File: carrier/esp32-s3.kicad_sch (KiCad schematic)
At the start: 16 parts, among them J1 USB_C_Receptacle_USB2.0, J5 ESP GPIO 1, J6 ESP GPIO 2, SW1 ESP RST, U2 ESP32-S3-MINI-1-N8, U5 TPD4EUSB30

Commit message: Feat[carrier]: v3 schematic draft complete
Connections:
- net USB2_N is gone; now on net USB_P: U5.4 (D2+), U5.7
- net USB2_P is gone; now on net USB_N: U5.5 (D2-), U5.6
- net ADC2_CH4: now reaches U2.19 (IO15)
- net ADC1_CH4: now reaches U2.9 (IO5)
- no-connect marks 28 -> 26
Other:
- moved on the sheet: C5, C6, C7, C8, C9, J1, J5, J6, R2, R3, R5, R8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

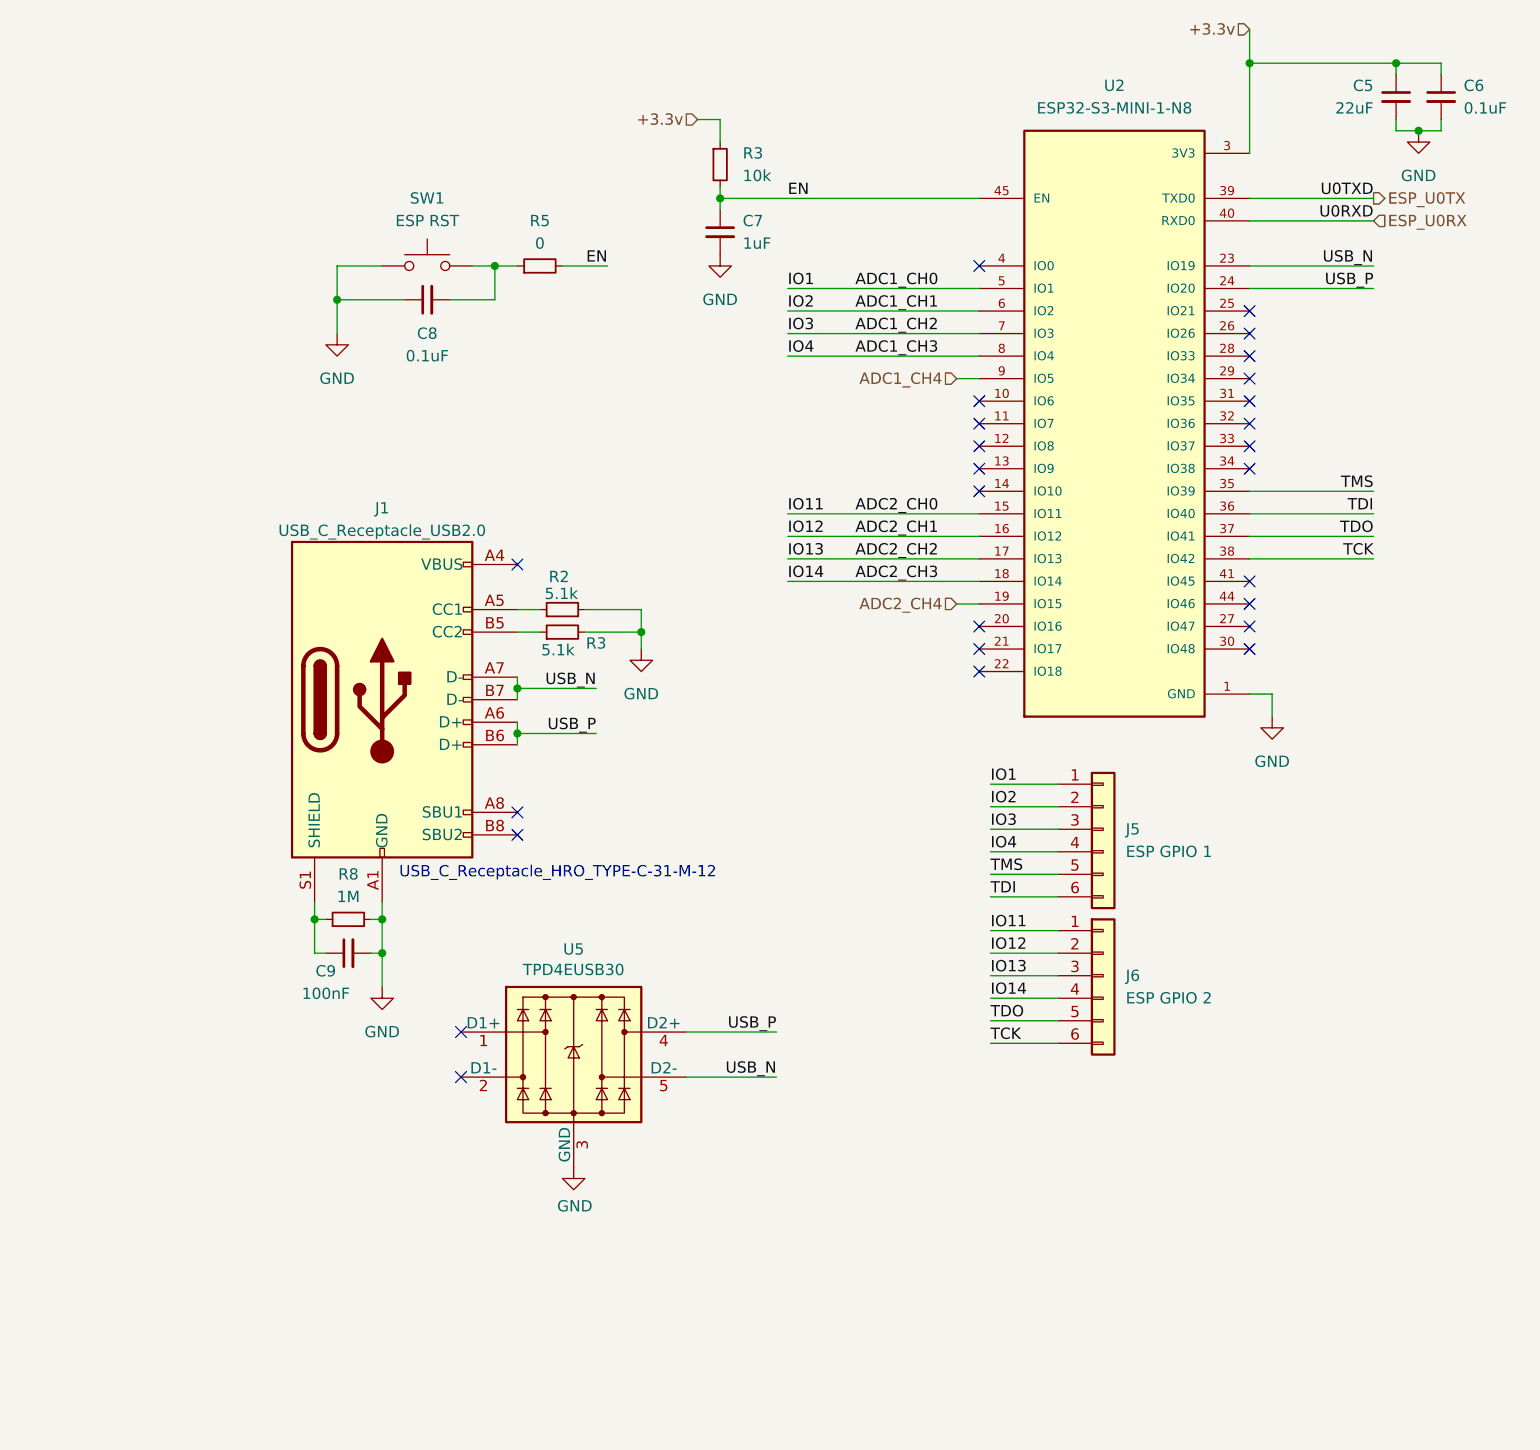
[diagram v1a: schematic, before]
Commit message: Feat[carrier]: implemented external magnetics, footprints linked
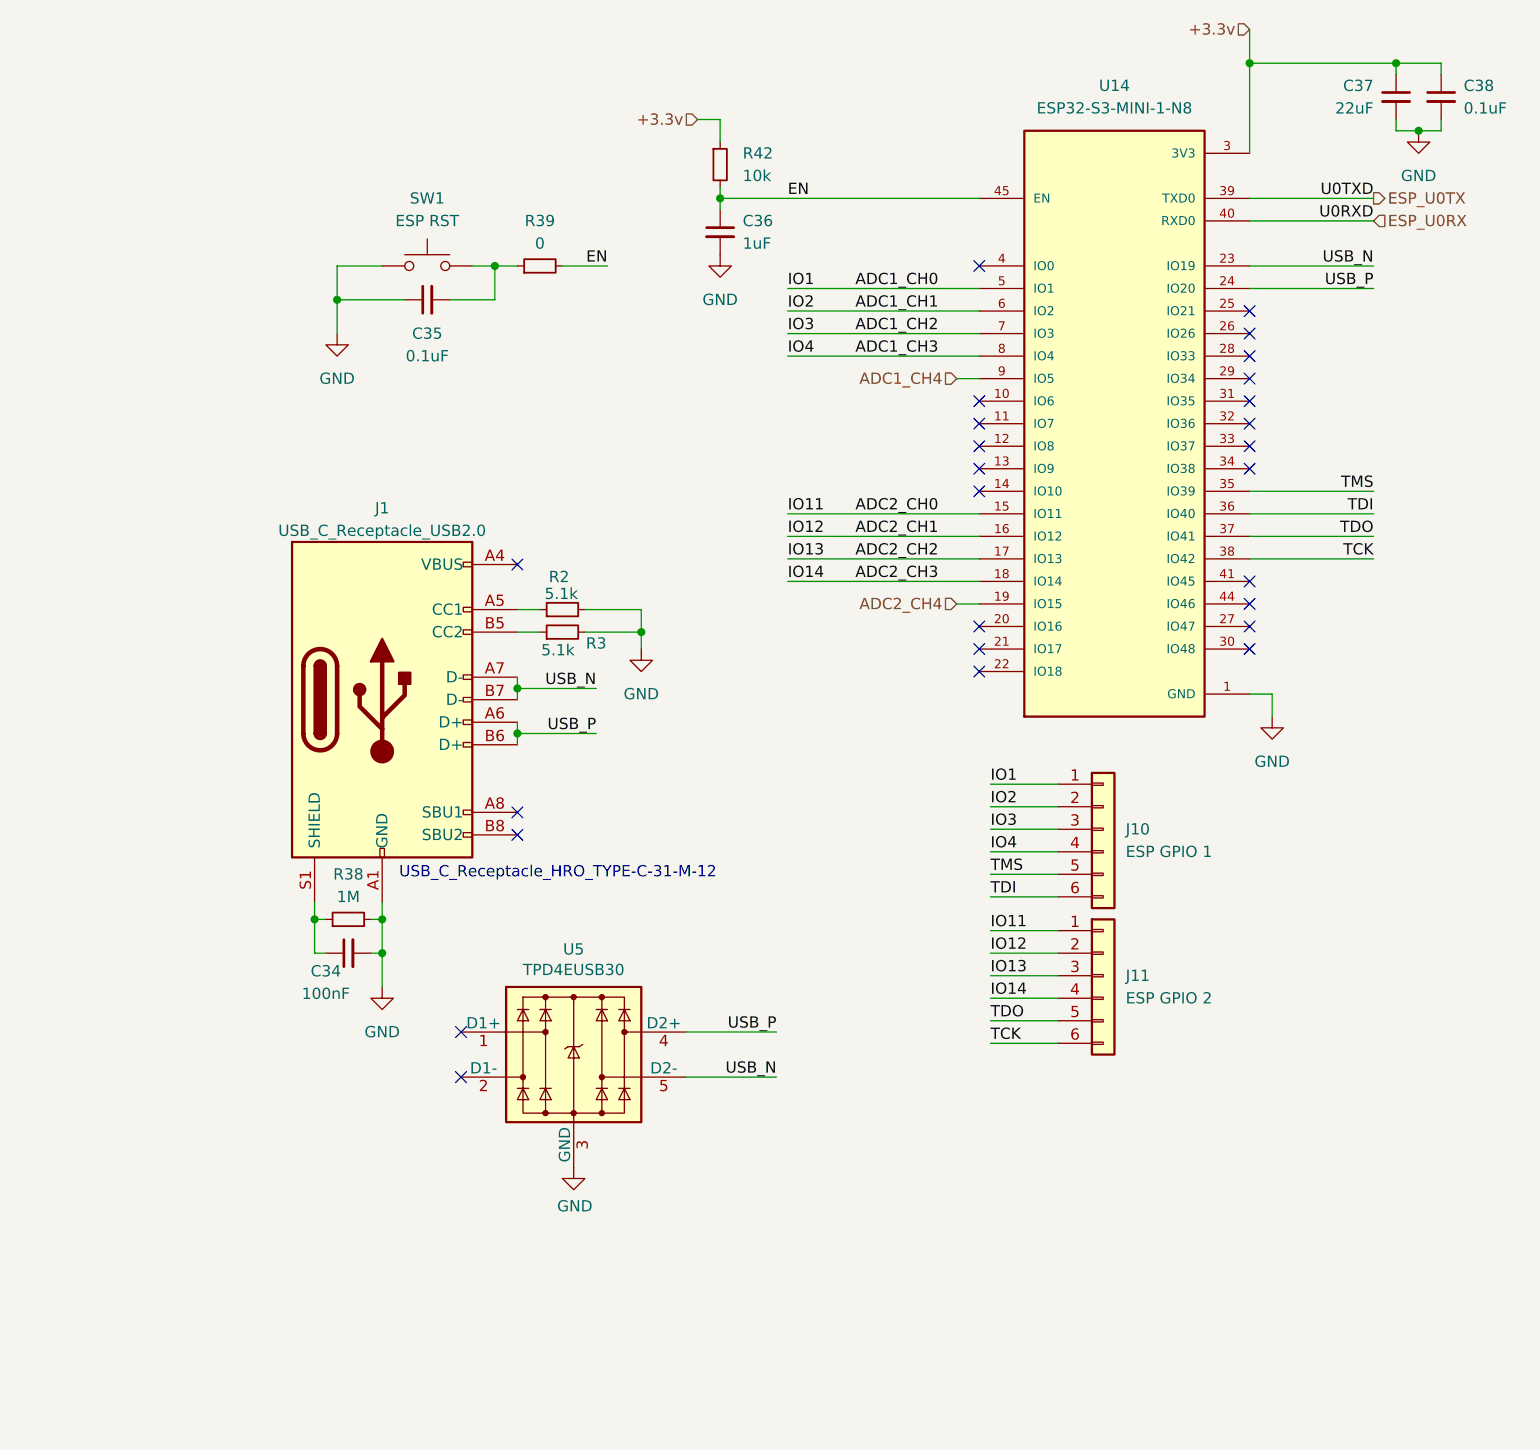
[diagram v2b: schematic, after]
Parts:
- C34: renamed from C9; footprint (none) -> Capacitor_SMD:C_0402_1005Metric
- C35: renamed from C8; footprint (none) -> Capacitor_SMD:C_0402_1005Metric
- C36: renamed from C7; footprint (none) -> Capacitor_SMD:C_0402_1005Metric
- C37: renamed from C5; footprint (none) -> Capacitor_SMD:C_0402_1005Metric
- C38: renamed from C6; footprint (none) -> Capacitor_SMD:C_0402_1005Metric
- J10: renamed from J5; footprint (none) -> Connector_PinHeader_2.54mm:PinHeader_1x06_P2.54mm_Vertical_SMD_Pin1Left
- J11: renamed from J6; footprint (none) -> Connector_PinHeader_2.54mm:PinHeader_1x06_P2.54mm_Vertical_SMD_Pin1Left
- R38: renamed from R8; footprint (none) -> Resistor_SMD:R_0402_1005Metric
- R39: renamed from R5; footprint (none) -> Resistor_SMD:R_0402_1005Metric
- R42: renamed from R3; footprint (none) -> Resistor_SMD:R_0402_1005Metric
- SW1: footprint (none) -> Button_Switch_SMD:SW_Push_1P1T_XKB_TS-1187A
- U14: renamed from U2; footprint ESP32-S3-MINI-1-N8:XCVR_ESP32-S3-MINI-1-N8 -> ESP32-S3-MINI-1:ESP32-S3-MINI-1

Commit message: Feat[carrier]: v3 board layout complete
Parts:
- J10, J11: footprint Connector_PinHeader_2.54mm:PinHeader_1x06_P2.54mm_Vertical_SMD_Pin1Left -> Connector_PinHeader_2.54mm:PinHeader_1x06_P2.54mm_Vertical
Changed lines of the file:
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@@
       (effects (font (size 1.27 1.27)) (justify left))
     )
-    (property "Footprint" "Connector_PinHeader_2.54mm:PinHeader_1x06_P2.54mm_Vertical_SMD_Pin1Left" (at 153.67 125.73 0)
+    (property "Footprint" "Connector_PinHeader_2.54mm:PinHeader_1x06_P2.54mm_Vertical" (at 153.67 125.73 0)
       (effects (font (size 1.27 1.27)) hide)
     )
@@
       (effects (font (size 1.27 1.27)) (justify left))
     )
-    (property "Footprint" "Connector_PinHeader_2.54mm:PinHeader_1x06_P2.54mm_Vertical_SMD_Pin1Left" (at 153.67 142.24 0)
-      (effects (font (size 1.27 1.27)) hide)
-    )
+    (property "Footprint" "Connector_PinHeader_2.54mm:PinHeader_1x06_P2.54mm_Vertical" (at 153.67 142.24 0)
+      (effects (font (size 1.27 1.27)) hide)
+    )

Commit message: Feat[carrier]: component mapping complete
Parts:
- C37: footprint Capacitor_SMD:C_0402_1005Metric -> Capacitor_SMD:C_0603_1608Metric
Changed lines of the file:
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@@
       (effects (font (size 1.27 1.27)) (justify right))
     )
-    (property "Footprint" "Capacitor_SMD:C_0402_1005Metric" (at 186.69 43.18 0)
+    (property "Footprint" "Capacitor_SMD:C_0603_1608Metric" (at 186.69 43.18 0)
       (effects (font (size 1.27 1.27)) hide)
     )

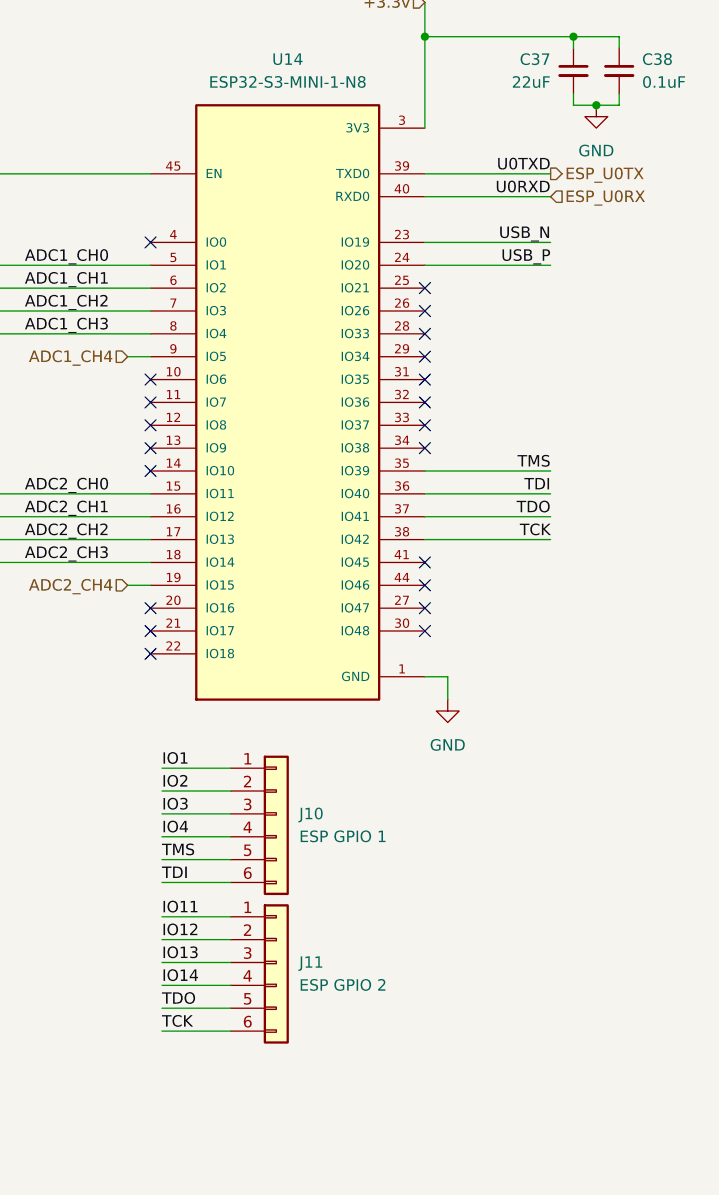
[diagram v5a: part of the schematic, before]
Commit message: Fix: updated carrier board to v3.1
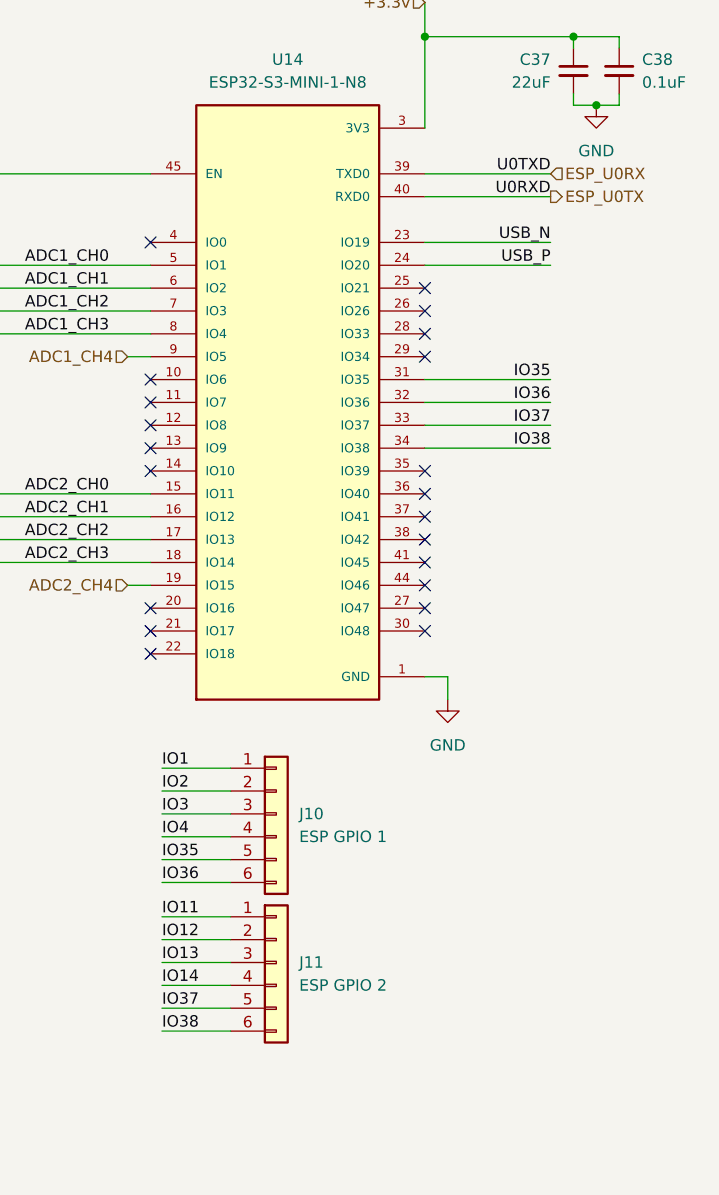
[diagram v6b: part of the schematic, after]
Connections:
- net ESP_U0RX: now also U14.39 (TXD0); no longer U14.40 (RXD0)
- net ESP_U0TX: now also U14.40 (RXD0); no longer U14.39 (TXD0)
- net IO35: now reaches U14.31 (IO35)
- net IO35: now also J10.5 (Pin_5)
- net IO36: now reaches U14.32 (IO36)
- net IO36: now also J10.6 (Pin_6)
- net IO37: now reaches U14.33 (IO37)
- net IO37: now also J11.5 (Pin_5)
- net IO38: now reaches U14.34 (IO38)
- net IO38: now also J11.6 (Pin_6)
- net TCK: no longer names the net of U14.38 (IO42)
- net TCK: no longer J11.6 (Pin_6)
- net TDI: no longer names the net of U14.36 (IO40)
- net TDI: no longer J10.6 (Pin_6)
- net TDO: no longer names the net of U14.37 (IO41)
- net TDO: no longer J11.5 (Pin_5)
- net TMS: no longer names the net of U14.35 (IO39)
- net TMS: no longer J10.5 (Pin_5)
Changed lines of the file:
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@@
   (title_block
     (title "Carrier Board")
-    (date "2023-12-09")
-    (rev "V3")
+    (date "2023-12-30")
+    (rev "V3.1")
     (company "MUREX Robotics [Byran Huang]")
     (comment 1 "//DO IT RIGHT,  DO IT MUREX")
@@
   (no_connect (at 139.7 77.47))
   (no_connect (at 170.18 74.93))
-  (no_connect (at 170.18 82.55))
+  (no_connect (at 170.18 90.17))
   (no_connect (at 139.7 85.09))
+  (no_connect (at 170.18 87.63))
   (no_connect (at 139.7 105.41))
   (no_connect (at 87.63 95.885))
   (no_connect (at 170.18 100.33))
+  (no_connect (at 170.18 92.71))
   (no_connect (at 170.18 67.31))
   (no_connect (at 170.18 69.85))
   (no_connect (at 170.18 102.87))
-  (no_connect (at 170.18 77.47))
-  (no_connect (at 170.18 85.09))
   (no_connect (at 139.7 107.95))
   (no_connect (at 139.7 80.01))
-  (no_connect (at 170.18 80.01))
   (no_connect (at 139.7 87.63))
+  (no_connect (at 170.18 95.25))
   (no_connect (at 170.18 105.41))
   (no_connect (at 87.63 126.365))
@@
     (stroke (width 0) (type default))
   )
-  (wire (pts (xy 170.18 87.63) (xy 184.15 87.63))
+  (wire (pts (xy 170.18 77.47) (xy 184.15 77.47))
     (stroke (width 0) (type default))
   )
@@
     (stroke (width 0) (type default))
   )
-  (wire (pts (xy 170.18 90.17) (xy 184.15 90.17))
+  (wire (pts (xy 170.18 80.01) (xy 184.15 80.01))
     (stroke (width 0) (type default))
   )
@@
     (stroke (width 0) (type default))
   )
-  (wire (pts (xy 170.18 92.71) (xy 184.15 92.71))
-    (stroke (width 0) (type default))
-  )
-  (wire (pts (xy 170.18 95.25) (xy 184.15 95.25))
+  (wire (pts (xy 170.18 82.55) (xy 184.15 82.55))
+    (stroke (width 0) (type default))
+  )
+  (wire (pts (xy 170.18 85.09) (xy 184.15 85.09))
     (stroke (width 0) (type default))
   )
@@
     (effects (font (size 1.27 1.27)) (justify left bottom))
   )
-  (label "TDO" (at 140.97 147.32 0) (fields_autoplaced)
-    (effects (font (size 1.27 1.27)) (justify left bottom))
-  )
-  (label "TCK" (at 184.15 95.25 180) (fields_autoplaced)
+  (label "IO37" (at 140.97 147.32 0) (fields_autoplaced)
+    (effects (font (size 1.27 1.27)) (justify left bottom))
+  )
+  (label "IO38" (at 184.15 85.09 180) (fields_autoplaced)
     (effects (font (size 1.27 1.27)) (justify right bottom))
   )
@@
     (effects (font (size 1.27 1.27)) (justify left bottom))
   )
-  (label "TCK" (at 140.97 149.86 0) (fields_autoplaced)
-    (effects (font (size 1.27 1.27)) (justify left bottom))
-  )
-  (label "TDI" (at 184.15 90.17 180) (fields_autoplaced)
+  (label "IO38" (at 140.97 149.86 0) (fields_autoplaced)
+    (effects (font (size 1.27 1.27)) (justify left bottom))
+  )
+  (label "IO36" (at 184.15 80.01 180) (fields_autoplaced)
     (effects (font (size 1.27 1.27)) (justify right bottom))
   )
@@
     (effects (font (size 1.27 1.27)) (justify left bottom))
   )
-  (label "TMS" (at 184.15 87.63 180) (fields_autoplaced)
+  (label "IO35" (at 184.15 77.47 180) (fields_autoplaced)
     (effects (font (size 1.27 1.27)) (justify right bottom))
   )
@@
     (effects (font (size 1.27 1.27)) (justify left bottom))
   )
-  (label "TDO" (at 184.15 92.71 180) (fields_autoplaced)
+  (label "IO37" (at 184.15 82.55 180) (fields_autoplaced)
     (effects (font (size 1.27 1.27)) (justify right bottom))
   )
@@
     (effects (font (size 1.27 1.27)) (justify right bottom))
   )
-  (label "TMS" (at 140.97 130.81 0) (fields_autoplaced)
+  (label "IO35" (at 140.97 130.81 0) (fields_autoplaced)
     (effects (font (size 1.27 1.27)) (justify left bottom))
   )
@@
     (effects (font (size 1.27 1.27)) (justify left bottom))
   )
-  (label "TDI" (at 140.97 133.35 0) (fields_autoplaced)
+  (label "IO36" (at 140.97 133.35 0) (fields_autoplaced)
     (effects (font (size 1.27 1.27)) (justify left bottom))
   )
@@
     (effects (font (size 1.27 1.27)) (justify left bottom))
   )
-  (hierarchical_label "ESP_U0RX" (shape input) (at 184.15 57.15 0) (fields_autoplaced)
+  (hierarchical_label "ESP_U0RX" (shape input) (at 184.15 54.61 0) (fields_autoplaced)
     (effects (font (size 1.27 1.27)) (justify left))
   )
@@
     (effects (font (size 1.27 1.27)) (justify right))
   )
-  (hierarchical_label "ESP_U0TX" (shape output) (at 184.15 54.61 0) (fields_autoplaced)
+  (hierarchical_label "ESP_U0TX" (shape output) (at 184.15 57.15 0) (fields_autoplaced)
     (effects (font (size 1.27 1.27)) (justify left))
   )

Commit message: Feat: float sid
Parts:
- renumbered U5 to U13
